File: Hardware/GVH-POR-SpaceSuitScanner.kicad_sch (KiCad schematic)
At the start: 12 parts, among them J1 Conn_01x04, U1 AW9523, U2 AW9523, U3 AT42QT1010-TSHR

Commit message: A ton of PCB Work
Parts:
- removed J1: Conn_01x04, symbol Connector_Generic:Conn_01x04
- added C3: 10uF, Capacitor_SMD:C_0805_2012Metric_Pad1.18x1.45mm_HandSolder, symbol Device:C_Small
- added C4: 0.1uF, Capacitor_SMD:C_0805_2012Metric_Pad1.18x1.45mm_HandSolder, symbol Device:C_Small
- added C5: 22nF, Capacitor_SMD:C_0805_2012Metric, symbol Device:C_Small
- added C6: 0.1uF, Capacitor_SMD:C_0805_2012Metric, symbol Device:C_Small
- added D1: LED_Small, LED_SMD:LED_0805_2012Metric_Pad1.15x1.40mm_HandSolder, symbol Device:LED_Small
- added D2: 1N4148, Diode_SMD:D_SOD-123, symbol Device:D
- added D3: LED, LED_SMD:LED_0805_2012Metric_Pad1.15x1.40mm_HandSolder, symbol Device:LED
- added J1, J10, J11, J12, J13, J14, J15, J16, J17, J18, J19, J2, J20, J21, J22, J23, J24, J25, J26, J3, J4, J5, J6, J7, J8, J9: Phoenix _725656, my_footprints:PHOENIX_1725656, symbol my_library:Phoenix _725656
- added J27: Touch, my_footprints:PHOENIX_1725656, symbol my_library:Phoenix _725656
- added J28: n00d +, my_footprints:PHOENIX_1725656, symbol my_library:Phoenix _725656
- added J29: n00d i2c, my_footprints:MOLEX_MICROFIT-RA-4POS, symbol my_library:Molex Micro-Fit 4pos
- added J30: Matrix i2c, my_footprints:MOLEX_MICROFIT-RA-4POS, symbol my_library:Molex Micro-Fit 4pos
- added J31: Speaker In, my_footprints:MOLEX_MICROFIT-RA-2POS, symbol my_library:Molex Micro-Fit 2pos
- added J32: Speaker, Connector_PinSocket_2.54mm:PinSocket_1x02_P2.54mm_Horizontal, symbol Connector_Generic:Conn_01x02
- added K1: EC2-3NU, my_footprints:RELAY8_EE2-3NUH_KEM-M, symbol my_library:EC2-3NU
- added Q1: Q_NPN_BEC, Package_TO_SOT_SMD:SOT-23, symbol Device:Q_NPN_BEC
- added R6: 10K, Resistor_SMD:R_0805_2012Metric, symbol Device:R_Small
- added R7: 1K, Resistor_SMD:R_0805_2012Metric, symbol Device:R_Small
- added U3, U4: AW9523 Expander, my_footprints:Adafruit_AW9523_GPIO_Expander, symbol my_library:Adafruit_AW9523_GPIO_Expander
- added U6: IS31FL3731 LED Driver, my_footprints:Adafruit IS31FL3731 LED Driver, symbol my_library:Adafruit_IS31FL3731_Matrix
- C1, C2: footprint (none) -> Capacitor_SMD:C_0805_2012Metric_Pad1.18x1.45mm_HandSolder
- R1, R2: footprint (none) -> Resistor_SMD:R_0805_2012Metric_Pad1.20x1.40mm_HandSolder
- R3: value 10k -> 10K; footprint (none) -> Resistor_SMD:R_0805_2012Metric
- R4, R5: value 10k -> 1K; footprint (none) -> Resistor_SMD:R_0805_2012Metric
- U5: renamed from U3; value AT42QT1010-TSHR -> AT42QT1010; Digikey Page (none) -> https://www.digikey.com/en/products/detail/microchip-techno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
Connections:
- net +3.3V is gone; now on net VCC: C1.1, C2.1, U1.21 (VDD), U2.21 (VDD)
- net GND: now also R4.1, U1.18 (A0), U1.24 (A1), U1.25 (GND), U2.24 (A1), U2.25 (GND), U5.2 (VSS), C3.2, C4.2, C6.2, J29.1 (Pin_1), J30.1 (Pin_1), Q1.2 (E), R6.2, U3.13 (GND), U4.13 (GND), U6.2 (GND)
- net NOOD_SCL: now also R2.1, U1.19 (SCL), J29.4 (Pin_4), U3.14 (SCL), U4.14 (SCL)
- net NOOD_SDA: now also R1.1, U1.20 (SDA), J29.3 (Pin_3), U3.15 (SDA), U4.15 (SDA)
- net TOUCH_OUT: now reaches U5.1 (OUT)
- net TOUCH_OUT: now also D1.2 (A)
- net at U5.3 (SNSK): now also R3.2, C5.1
- net at U5.4 (SNS): now also C5.2
- net VCC: now reaches U5.5 (VDD)
- net VCC: now also R1.2, R2.2, U1.23 (~{RST}), U2.18 (A0), U2.23 (~{RST}), U5.6 (SYNC), C3.1, C4.1, C6.1, D2.1 (K), J29.2 (Pin_2), J30.2 (Pin_2), K1.1, K1.4, R7.1, U3.12 (VIN), U4.12 (VIN), U6.1 (VCC)
- net at R3.1: now also J27.1, J27.2
- net P12_0: now reaches U2.1 (P1_0)
- net P12_0: now also U4.18 (8)
- net P02_4: now reaches U2.10 (P0_4)
- net P02_4: now also U4.4
- net P02_5: now reaches U2.11 (P0_5)
- net P02_5: now also U4.5
- net P02_6: now reaches U2.12 (P0_6)
- net P02_6: now also U4.6
- net P02_7: now reaches U2.13 (P0_7)
- net P02_7: now also U4.7
- net P12_4: now reaches U2.14 (P1_4)
- net P12_4: now also U4.8 (12)
- net P12_5: now reaches U2.15 (P1_5)
- net P12_5: now also U4.9 (13)
- net P12_6: now reaches U2.16 (P1_6)
- net P12_6: now also U4.10 (14)
- net P12_7: now reaches U2.17 (P1_7)
- net P12_7: now also U4.11 (15)
- net P12_1: now reaches U2.2 (P1_1)
- net P12_1: now also U4.19 (9)
- net P12_2: now reaches U2.3 (P1_2)
- net P12_2: now also U4.20 (10)
- net P12_3: now reaches U2.4 (P1_3)
- net P12_3: now also U4.21 (11)
- net P02_0: now reaches U2.5 (P0_0)
- net P02_0: now also U4.1, U4.22 (0)
- net P02_1: now reaches U2.6 (P0_1)
- net P02_2: now reaches U2.7 (P0_2)
- net P02_2: now also U4.2
- net P02_3: now reaches U2.8 (P0_3)
- net P02_3: now also U4.3
- net at R5.1: now also Q1.1 (B), R6.1
- net RELAY: now reaches R5.2
- net at R4.2: now also D1.1 (K)
- net P11_0: now reaches U1.1 (P1_0)
- net P11_0: now also U3.18 (8)
- net P01_4: now reaches U1.10 (P0_4)
- net P01_4: now also U3.4
- net P01_5: now reaches U1.11 (P0_5)
- net P01_5: now also U3.5
- net P01_6: now reaches U1.12 (P0_6)
- net P01_6: now also U3.6
- net P01_7: now reaches U1.13 (P0_7)
- net P01_7: now also U3.7
- net P11_4: now reaches U1.14 (P1_4)
- net P11_4: now also U3.8 (12)
- net P11_5: now reaches U1.15 (P1_5)
- net P11_5: now also U3.9 (13)
- net P11_6: now reaches U1.16 (P1_6)
- net P11_6: now also U3.10 (14)
- net P11_7: now reaches U1.17 (P1_7)
- net P11_7: now also U3.11 (15)
- net P11_1: now reaches U1.2 (P1_1)
- net P11_1: now also U3.19 (9)
- net P11_2: now reaches U1.3 (P1_2)
- net P11_2: now also U3.20 (10)
- net P11_3: now reaches U1.4 (P1_3)
- net P11_3: now also U3.21 (11)
- net P01_0: now reaches U1.5 (P0_0)
- net P01_0: now also U3.22 (0)
- net P01_1: now reaches U1.6 (P0_1)
- net P01_1: now also U3.1
- net P01_2: now reaches U1.7 (P0_2)
- net P01_2: now also U3.2
- net P01_3: now reaches U1.8 (P0_3)
- net P01_3: now also U3.3
- new net: J31.1 (Pin_1), J32.1 (Pin_1)
- new net: J31.2 (Pin_2), J32.2 (Pin_2)
- new net: D2.2 (A), D3.1 (K), K1.12, Q1.3 (C)
- new net: D3.2 (A), R7.2
- new net: J28.1, K1.5
- new net MATRIX_SCL: J30.4 (Pin_4), U6.3 (SCL)
- new net MATRIX_SDA: J30.3 (Pin_3), U6.4 (SDA)
- no-connect marks 0 -> 28
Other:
- moved on the sheet: C1, C2, R1, R2, U5

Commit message: Schematic progress
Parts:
- removed J10, J11, J12, J13, J14, J15, J16, J17, J18, J19, J2, J20, J21, J22, J23, J24, J25, J26, J3, J4, J5, J6, J7, J8, J9: Phoenix _725656, my_footprints:PHOENIX_1725656, symbol my_library:Phoenix _725656
- removed J27: Touch, my_footprints:PHOENIX_1725656, symbol my_library:Phoenix _725656
- removed J28: n00d +, my_footprints:PHOENIX_1725656, symbol my_library:Phoenix _725656
- added D4, D5: LED_Small, LED_SMD:LED_0805_2012Metric_Pad1.15x1.40mm_HandSolder, symbol Device:LED_Small
- added J10: Phoenix_5POS_1725685, my_footprints:PHOENIX_1725685-5POS, symbol my_library:Phoenix_5POS_1725685
- added J11, J12, J13, J14, J15, J16, J17, J18, J2, J3, J4, J5, J6, J7, J8, J9: Phoenix _725656, my_footprints:PHOENIX_1725656-2POS, symbol my_library:Phoenix_2POS_725656
- added J19: Phoenix_3POS_1725669, my_footprints:PHOENIX_1725669-3POS, symbol my_library:Phoenix_3POS_1725669
- added JP1, JP2: SolderJumper_2_Open, Jumper:SolderJumper-2_P1.3mm_Open_TrianglePad1.0x1.5mm, symbol Jumper:SolderJumper_2_Open
- added R8, R9: 220, Resistor_SMD:R_0805_2012Metric, symbol Device:R_Small
- J1: footprint my_footprints:PHOENIX_1725656 -> my_footprints:PHOENIX_1725656-2POS; symbol my_library:Phoenix _725656 -> my_library:Phoenix_2POS_725656
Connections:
- net GND: no longer U1.2 (P1_1), U2.2 (P1_1)
- net VCC: now also D4.2 (A), D5.2 (A)
- new net: JP1.1 (A), R8.1
- new net: D4.1 (K), JP1.2 (B), R8.2
- new net: D5.1 (K), JP2.2 (B), R9.2
- new net: JP2.1 (A), R9.1
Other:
- moved on the sheet: C5, C6, D1, D2, D3, J1, J30, K1, Q1, R3, R4, R5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

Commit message: Continuing PCB Layout Process
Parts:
- removed D2: 1N4148, Diode_SMD:D_SOD-123, symbol Device:D
- removed D3: LED, LED_SMD:LED_0805_2012Metric_Pad1.15x1.40mm_HandSolder, symbol Device:LED
- removed K1: EC2-3NU, my_footprints:RELAY8_EE2-3NUH_KEM-M, symbol my_library:EC2-3NU
- removed Q1: Q_NPN_BEC, Package_TO_SOT_SMD:SOT-23, symbol Device:Q_NPN_BEC
- removed R5, R7: 1K, Resistor_SMD:R_0805_2012Metric, symbol Device:R_Small
- removed R6: 10K, Resistor_SMD:R_0805_2012Metric, symbol Device:R_Small
- C1, C3: symbol Device:C_Small -> Device:C_Polarized_Small
- D4, D5: footprint LED_SMD:LED_0805_2012Metric_Pad1.15x1.40mm_HandSolder -> LED_THT:LED_Rectangular_W5.0mm_H2.0mm
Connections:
- net P02_0: no longer U4.1
- net P02_1: now also U4.1

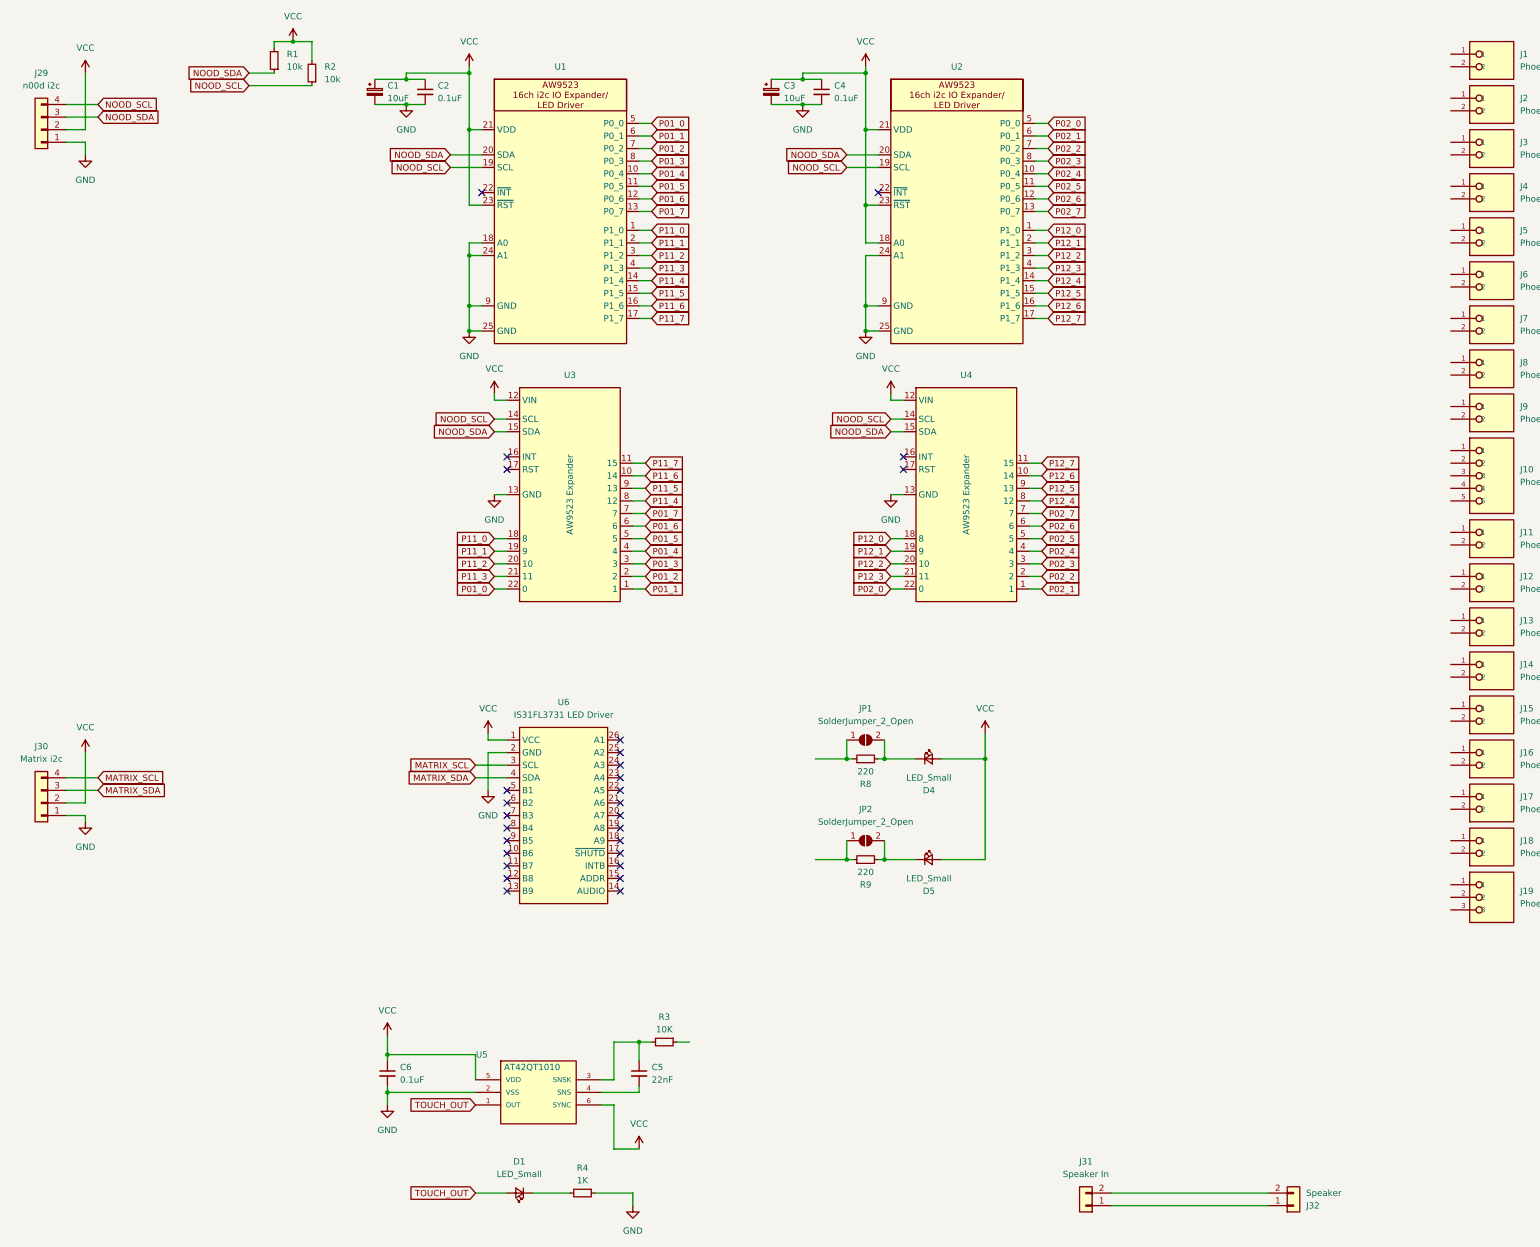
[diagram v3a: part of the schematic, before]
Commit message: Finished laying out PCB
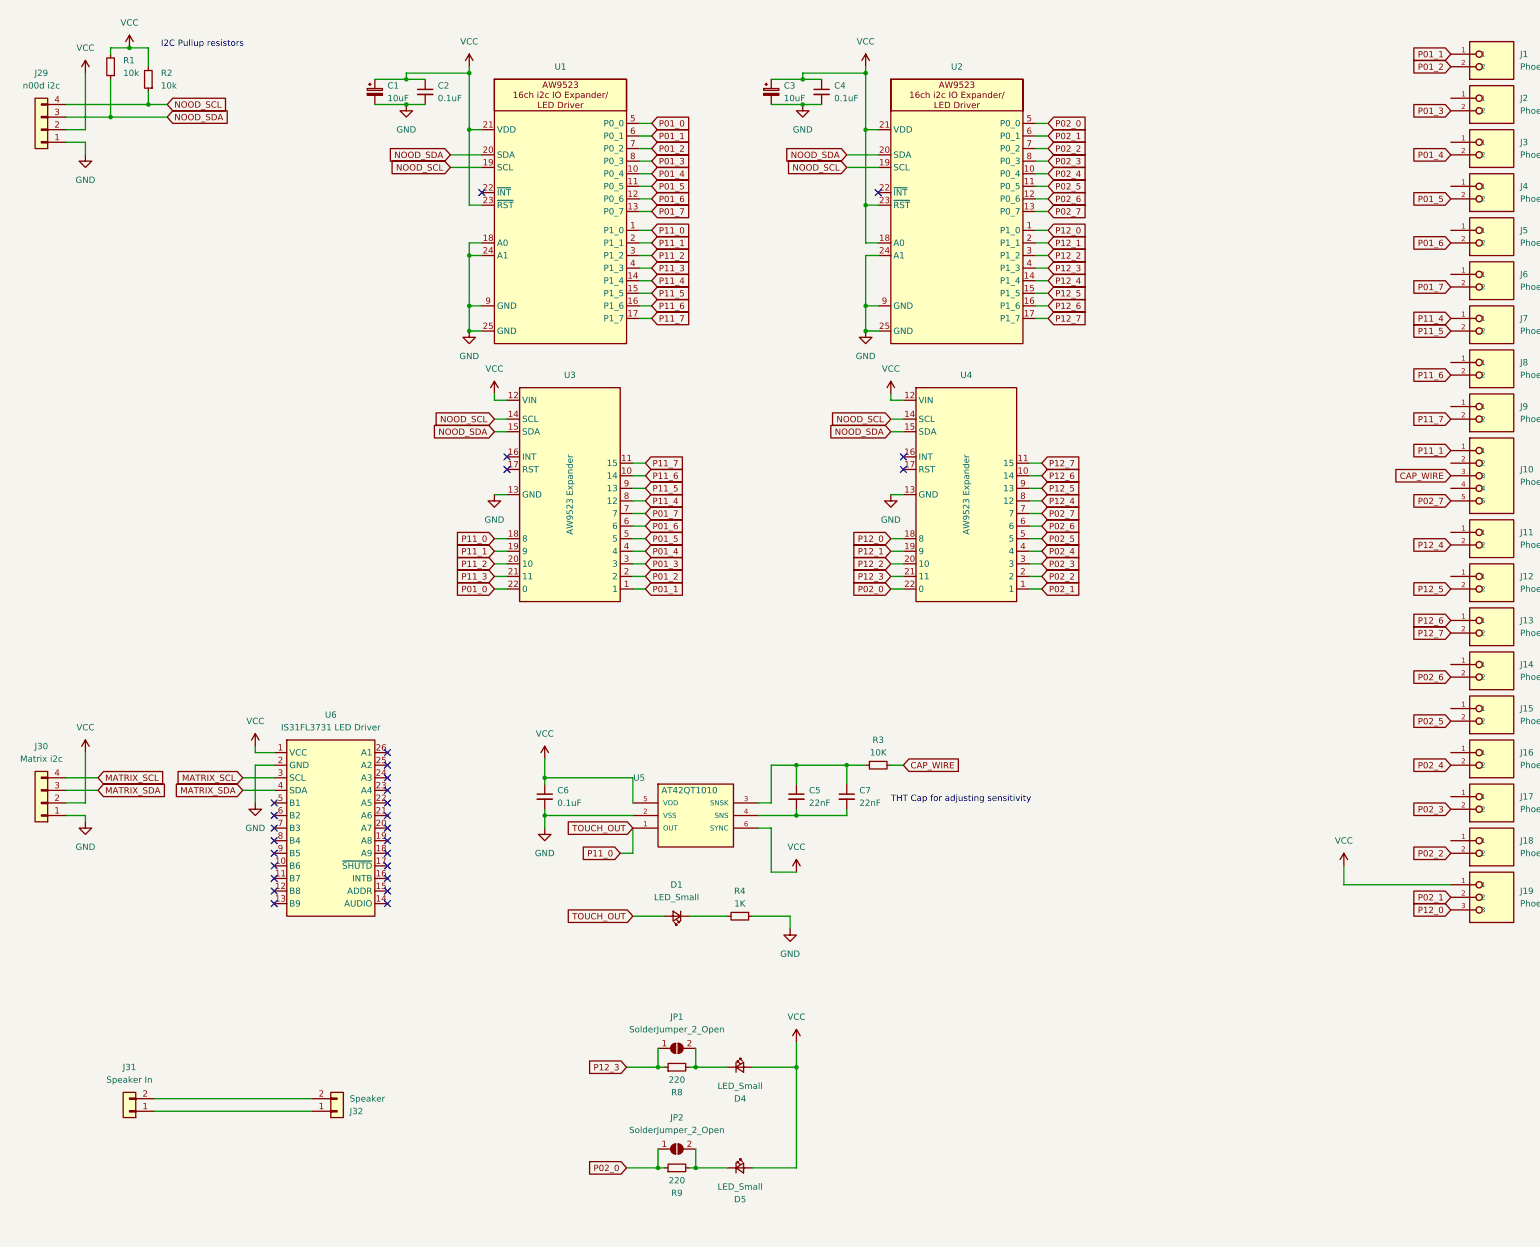
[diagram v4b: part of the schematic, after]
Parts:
- added C7: 22nF, Connector_PinHeader_2.54mm:PinHeader_1x02_P2.54mm_Vertical, symbol Device:C_Small
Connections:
- net TOUCH_OUT is gone; now on net P11_0: D1.2 (A), U5.1 (OUT)
- net P01_1: now also J1.1
- net P01_2: now also J1.2
- net P01_3: now also J2.2
- net P01_4: now also J3.2
- net P01_5: now also J4.2
- net P01_6: now also J5.2
- net P01_7: now also J6.2
- net P02_0: now also JP2.1 (A), R9.1
- net P02_1: now also J19.2
- net P02_2: now also J18.2
- net P02_3: now also J17.2
- net P02_4: now also J16.2
- net P02_5: now also J15.2
- net P02_6: now also J14.2
- net P02_7: now also J10.5
- net P11_1: now also J10.1
- net P11_4: now also J7.1
- net P11_5: now also J7.2
- net P11_6: now also J8.2
- net P11_7: now also J9.2
- net P12_0: now also J19.3
- net P12_3: now also JP1.1 (A), R8.1
- net P12_4: now also J11.2
- net P12_5: now also J12.2
- net P12_6: now also J13.1
- net P12_7: now also J13.2
- net VCC: now also J19.1
- net at C5.1, U5.3 (SNSK): now also R3.1, C7.1; no longer R3.2
- net at C5.2, U5.4 (SNS): now also C7.2
- net CAP_WIRE: now reaches J10.3
- net CAP_WIRE: now also R3.2
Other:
- note added: "I2C Pullup resistors"
- note added: "THT Cap for adjusting sensitivity"
- moved on the sheet: C5, C6, D1, D4, D5, J31, J32, JP1, JP2, R1, R2, R3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
